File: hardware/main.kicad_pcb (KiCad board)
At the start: 2 copper layers, 130 parts, among them J1 USB_DEBUG, J2 USB_TO_ANDROID, M1 Mounting Hole, M2 Mounting Hole, M3 Mounting Hole, M4 Mounting Hole, P1 VBAT-TEST, P11 MOTOR-R, P12 MOTOR-L, P13 AND5V, P14 P24, P2 USB-VBUS, P3 SERVO-TILT, P4 JTAG10, P5 POWER-CHARGE, P6 POWER, P7 BATCHG, P8 12VIN, P9 BAT, Q1 ZXMP2120FFTA, Q2 BD242CG, Q3 IRLML2803TRPBF, Q4 IRLML2803TRPBF, U1 STM32F102C6, U2 BQ24450, U3 ZLDO1117, U4 AP6502, U5 7408, U6 MC33926, U7 MC33926, U8 FT312D, X1 8MHz, X2 12MHz

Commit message: layout no unconnected
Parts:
- moved D2 157.9 mm to (180.4, 44.0), turned to 90 degrees
- moved R22 153.3 mm to (135.2, 57.4), turned to 180 degrees
- moved R21 151.5 mm to (180.4, 48.8), turned to 90 degrees
- moved C21 149.1 mm to (160.4, 64.6), turned to 270 degrees
- moved M4 144.2 mm to (114.3, 116.8)
- moved C15 140.4 mm to (168.8, 64.6), turned to 270 degrees
- moved L1 139.0 mm to (151.4, 64.2), turned to 270 degrees
- moved C1 136.6 mm to (148.0, 110.8)
- moved P6 135.8 mm to (157.0, 57.8)
- moved R23 135.5 mm to (144.4, 65.0)
- moved U4 134.9 mm to (137.4, 63.4)
- moved C17 134.4 mm to (125.8, 65.4), turned to 90 degrees
- moved C18 133.9 mm to (144.4, 60.2)
- moved C19 133.7 mm to (131.2, 63.8), turned to 270 degrees
- moved R44 131.3 mm to (159.5, 80.9), turned to 180 degrees
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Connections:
- P5 pad 1: /Power/VIN+ -> GND
- P5 pad 2: GND -> /Power/VIN+
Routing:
- net +3.3V: track 111.6 -> 364.4 mm, vias 5 -> 7
- net +5V: track 0.00 -> 139.8 mm, vias 0 -> 2
- net +24V: track 187.6 -> 290.6 mm
- net /JTDO: track 0.00 -> 79.9 mm, vias 0 -> 3
- net /JNTRST: track 0.00 -> 73.6 mm, vias 0 -> 3
- net /JTCK: track 0.00 -> 71.4 mm, vias 0 -> 5
- net /nRST: track 0.00 -> 64.1 mm, vias 0 -> 5
- net /JTMS: track 0.00 -> 62.6 mm, vias 0 -> 5
- net /JTDI: track 0.00 -> 60.8 mm, vias 0 -> 7
- net /Android/TX: track 0.00 -> 45.0 mm, vias 0 -> 4
- net /Android/RX: track 0.00 -> 42.7 mm, vias 0 -> 4
- net N-0000070: track 0.00 -> 42.2 mm
- net /AUX-PB6: track 0.00 -> 40.6 mm, vias 0 -> 4
- net /USB-DISCONNECT: track 0.00 -> 38.7 mm, vias 0 -> 2
- net N-0000048: track 0.00 -> 38.4 mm, vias 0 -> 2
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
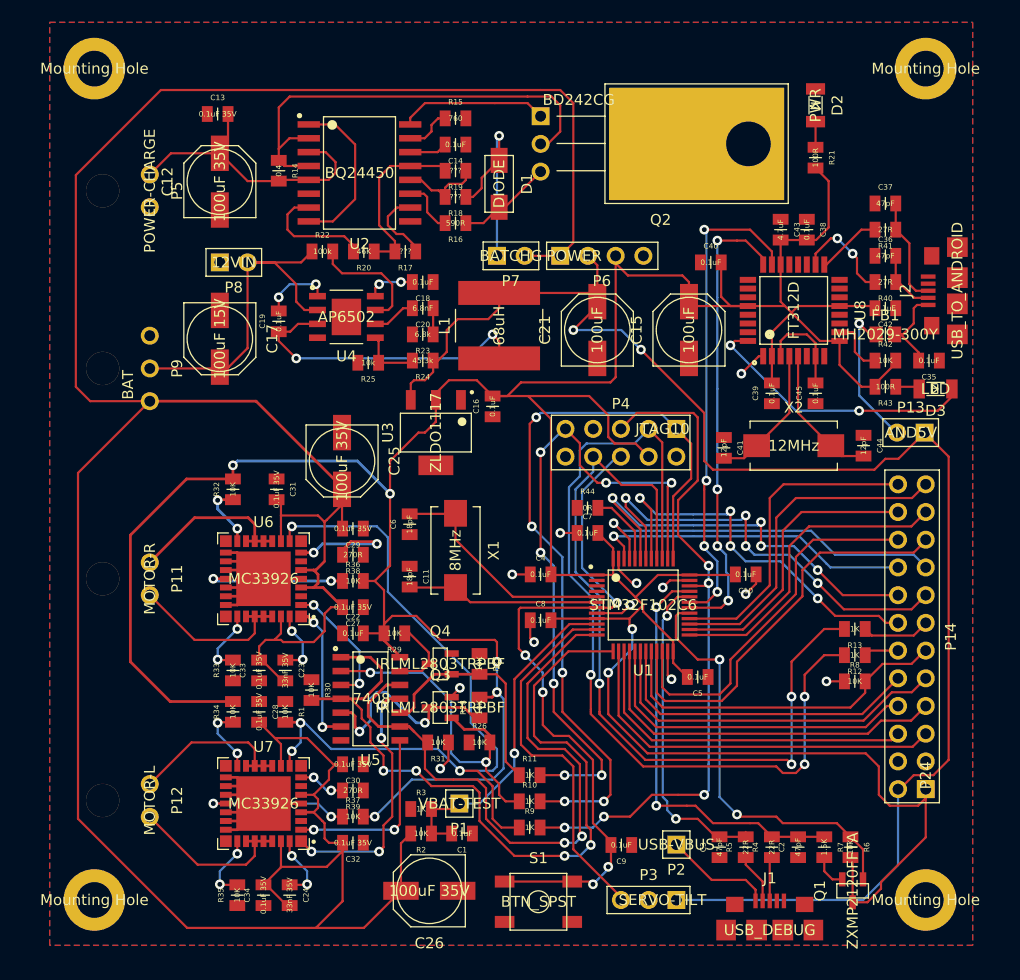
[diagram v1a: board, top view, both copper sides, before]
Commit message: added border and larger traces
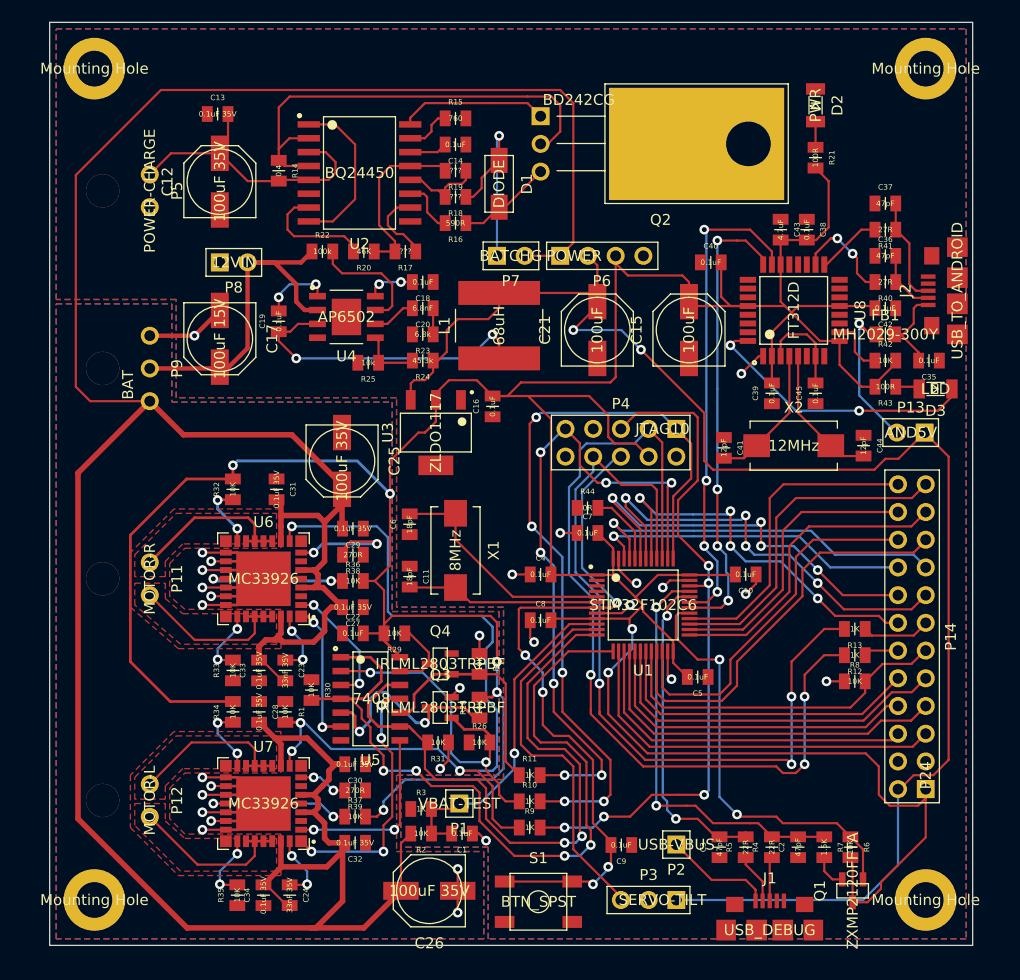
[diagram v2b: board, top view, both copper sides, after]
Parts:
- moved C30 0.20 mm to (138.2, 104.4)
- moved C32 0.20 mm to (138.2, 111.6)
- moved R37 0.20 mm to (138.2, 109.2)
- moved R39 0.20 mm to (138.2, 106.8)
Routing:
- net GND: track 83.9 -> 121.1 mm, vias 12 -> 29
- net /Motor Controllers/EN: track 71.1 -> 76.4 mm
- net +3.3V: track 364.4 -> 365.7 mm
- added copper zone on F.Cu, net /Motor Controllers/MOTOR-L-OUT1
- added copper zone on F.Cu, net /Motor Controllers/MOTOR-L-OUT2
- added copper zone on F.Cu, net /Motor Controllers/MOTOR-R-OUT1
- added copper zone on F.Cu, net /Motor Controllers/MOTOR-R-OUT2
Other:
- board outline added: 84.6 x 84.6 mm
- net class Power added: clearance 0.2032, trace_width 0.508, via_dia 0.889, via_drill 0.635
- net class Wide added: clearance 0.2032, trace_width 0.4064, via_dia 0.889, via_drill 0.635

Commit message: moved labels. increased power widths
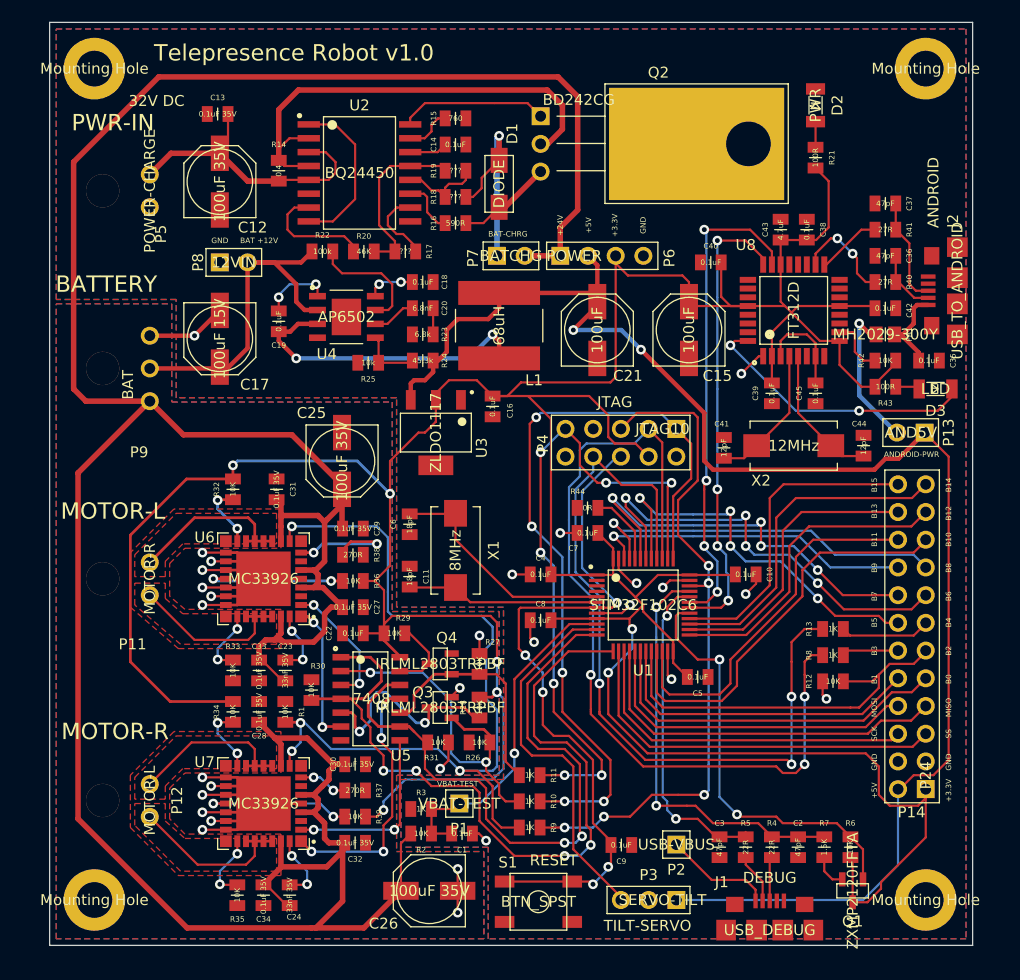
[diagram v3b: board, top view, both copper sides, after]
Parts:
- moved R12 2.00 mm to (182.0, 94.4)
- moved R13 2.00 mm to (182.0, 92.0)
- moved R8 2.00 mm to (182.0, 96.8)
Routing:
- net /AUX-PB2: track 32.5 -> 36.1 mm
- net +24V: track 290.8 -> 293.9 mm
- net /AUX-PB4: track 6.31 -> 8.31 mm
- net /AUX-PB3: track 3.18 -> 5.18 mm
- net N-0000070: track 42.2 -> 43.9 mm
- net /JTDO: track 79.9 -> 78.6 mm
- net /JNTRST: track 73.6 -> 72.6 mm
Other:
- board text added: "+24V"
- board text added: "+3.3V"
- board text added: "+5V"
- board text added: "32V DC"
- board text added: "ANDROID"
- board text added: "ANDROID-PWR"
- board text added: "B0"
- board text added: "B1"
- board text added: "B10"
- board text added: "B11"
- board text added: "B12"
- board text added: "B13"
- board text added: "B14"
- board text added: "B15"
- board text added: "B2"
- board text added: "B3"
- board text added: "B4"
- board text added: "B5"
- board text added: "B6"
- board text added: "B7"
- board text added: "B8"
- board text added: "B9"
- board text added: "BAT +12V"
- board text added: "BAT-CHRG"
- board text added: "BATTERY"
- board text added: "DEBUG"
- board text added: "GND"
- board text added: "JTAG"
- board text added: "MISO"
- board text added: "MOSI"
- board text added: "MOTOR-L"
- board text added: "MOTOR-R"
- board text added: "Open Hardware https://github.com/joeferner/ Designed By: Joe Ferner"
- board text added: "PWR-IN"
- board text added: "RESET"
- board text added: "SCK"
- board text added: "SS"
- board text added: "TILT-SERVO"
- board text added: "Telepresence Robot v1.0"
- board text added: "VBAT-TEST"

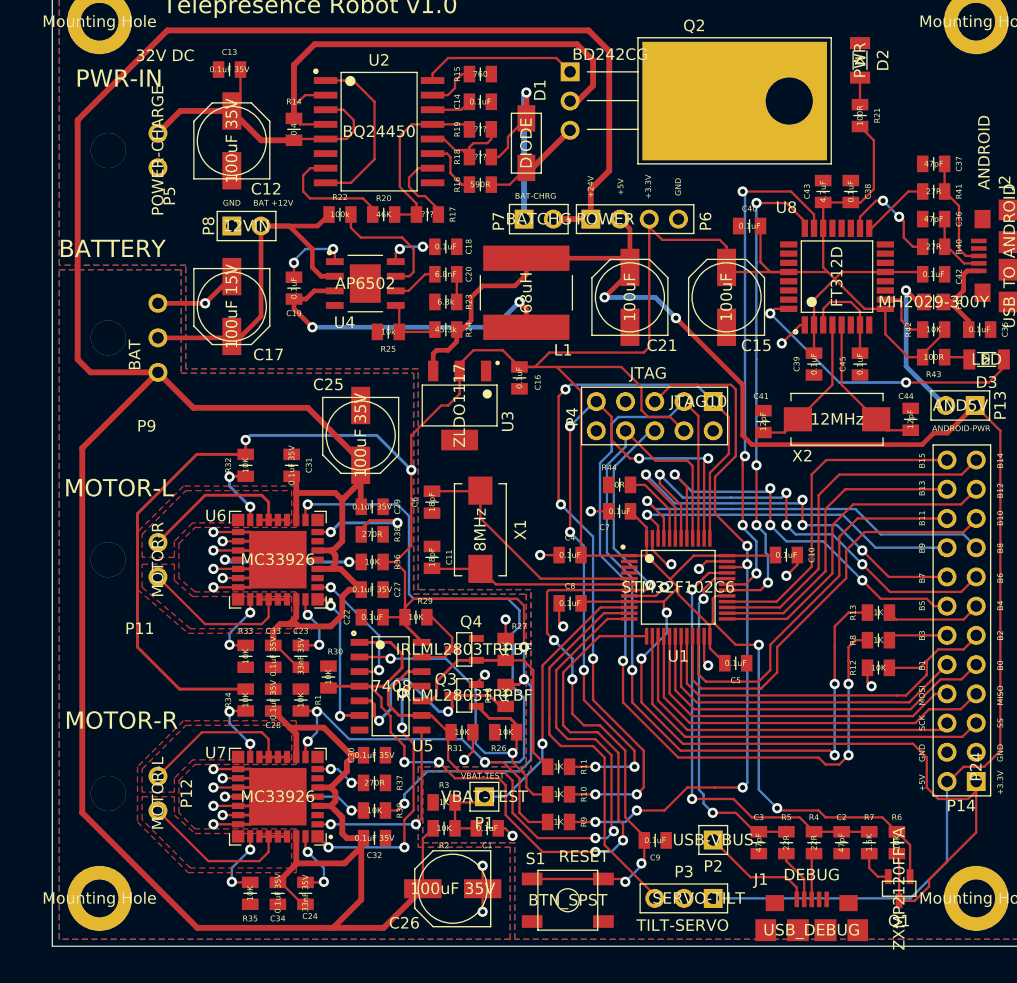
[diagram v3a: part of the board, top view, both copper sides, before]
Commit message: power track width, ground plane connects
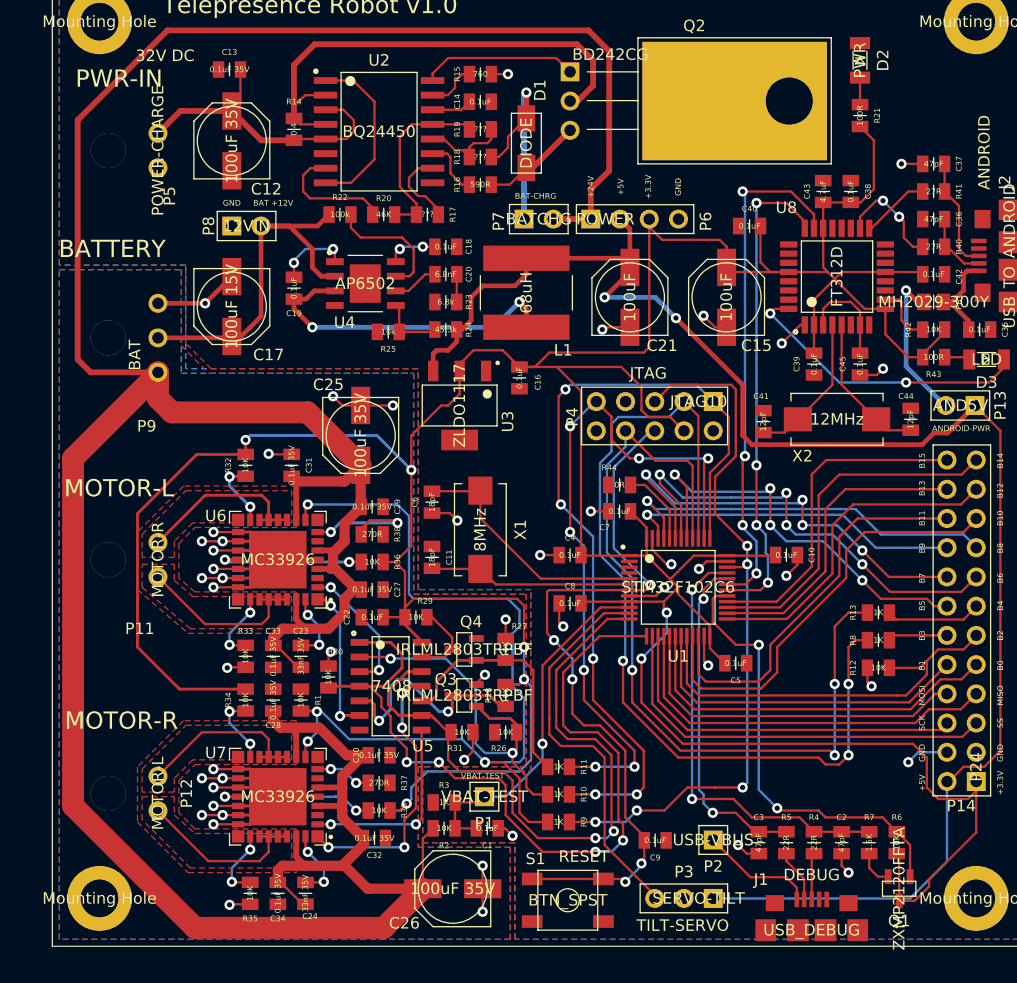
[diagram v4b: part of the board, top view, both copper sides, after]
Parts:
- moved C30 0.40 mm to (138.6, 104.4)
- moved R37 0.40 mm to (138.6, 109.2)
- moved R39 0.40 mm to (138.6, 106.8)
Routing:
- net GND: track 121.2 -> 161.3 mm, vias 29 -> 48
- net +24V: track 293.9 -> 296.5 mm
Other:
- net class MotorPower added: clearance 0.254, trace_width 1.905, via_dia 0.889, via_drill 0.635
- net class MotorPowerSingle added: clearance 0.254, trace_width 0.889, via_dia 0.889, via_drill 0.635
- net class MotorPowerSmaller added: clearance 0.254, trace_width 0.508, via_dia 0.889, via_drill 0.635
- net class Power removed
- net class Wide removed

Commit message: v1
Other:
- board text added: "Telepresence Robot 2013-09-03"
- board text removed: "Telepresence Robot v1.0"
